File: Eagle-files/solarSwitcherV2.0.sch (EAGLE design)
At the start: 12 parts, among them T1 2N3440

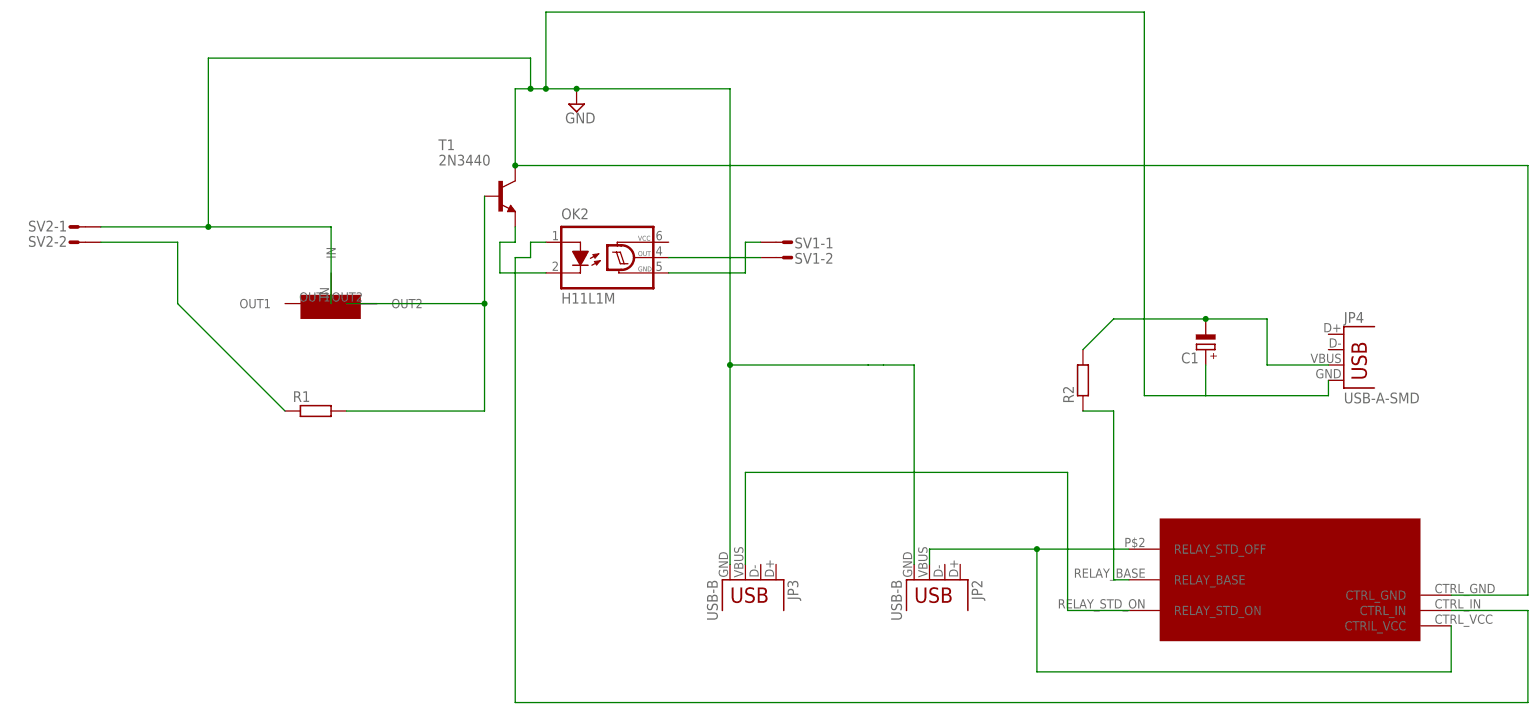
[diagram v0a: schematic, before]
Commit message: Removed relay-board and replaced with seperate relay and diode
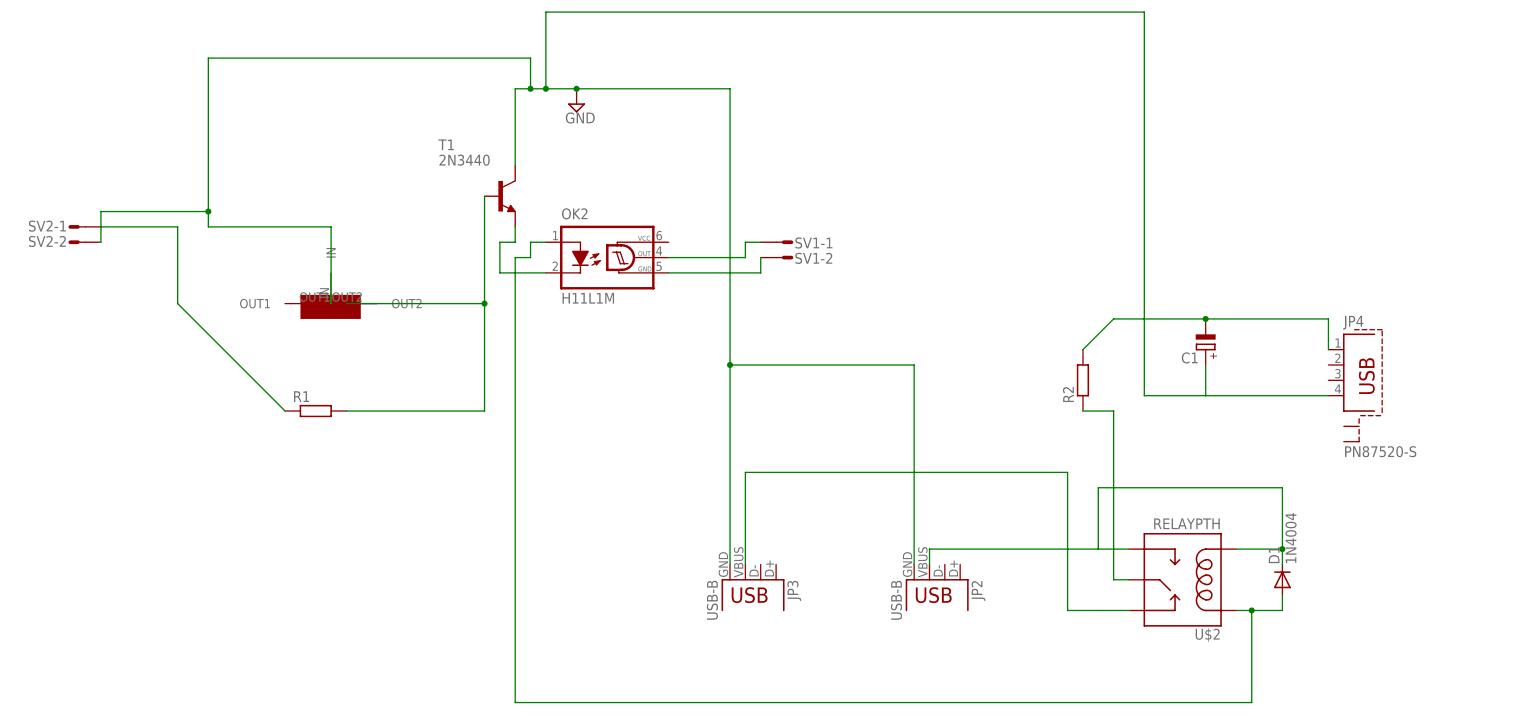
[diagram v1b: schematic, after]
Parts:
- removed U$1: RELAY_BOARD, MBLIB:RELAY_BOARD
- added D1: 1N4004, diode:1N4004
- added U$2: RELAYPTH, SRD-05VDC-SL-C:RELAYPTH
- JP4: value USB-A-SMD -> PN87520-S; device SparkFun-Connectors:USB-A-SMD -> con-berg:PN87520-S
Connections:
- removed net N$9: OK2.OUT, SV1-2.S
- new net N$12: D1.C, JP2.VBUS, U$2.COIL0, U$2.SWOPEN
- net GND: now also SV2-2.S; no longer JP4.GND, SV2-1.S, U$1.CTRL_GND
- net N$10: now also U$2.SWCOMMON; no longer U$1.RELAY_BASE
- net N$2: now also JP4.1; no longer JP4.VBUS
- net N$3: now also D1.A, U$2.COIL1; no longer U$1.CTRL_IN
- net N$4: now also OK2.OUT, SV1-1.S; no longer JP2.VBUS, U$1.CTRIL_VCC, U$1.RELAY_STD_OFF
- net N$5: now also SV2-1.S; no longer SV2-2.S
- net N$6: now also U$2.SWCLOSE; no longer U$1.RELAY_STD_ON
- net N$7: now also SV1-2.S; no longer SV1-1.S

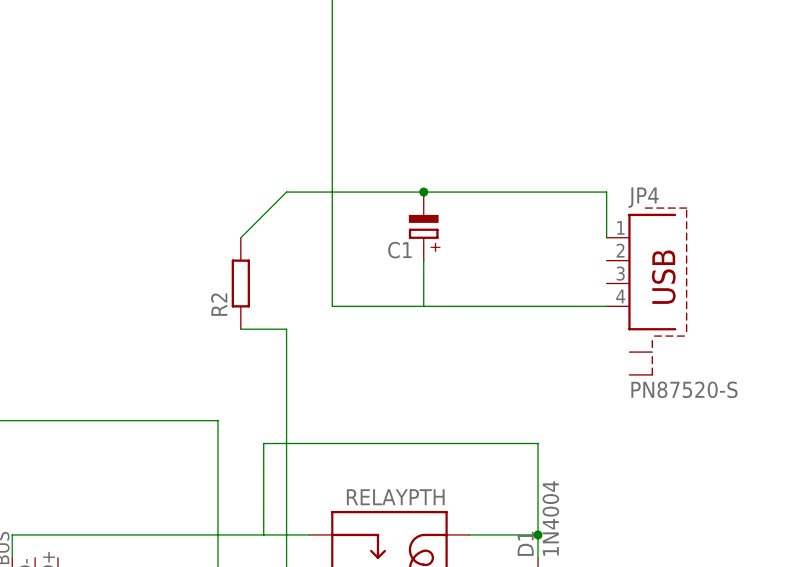
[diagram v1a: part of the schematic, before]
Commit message: Added status leds
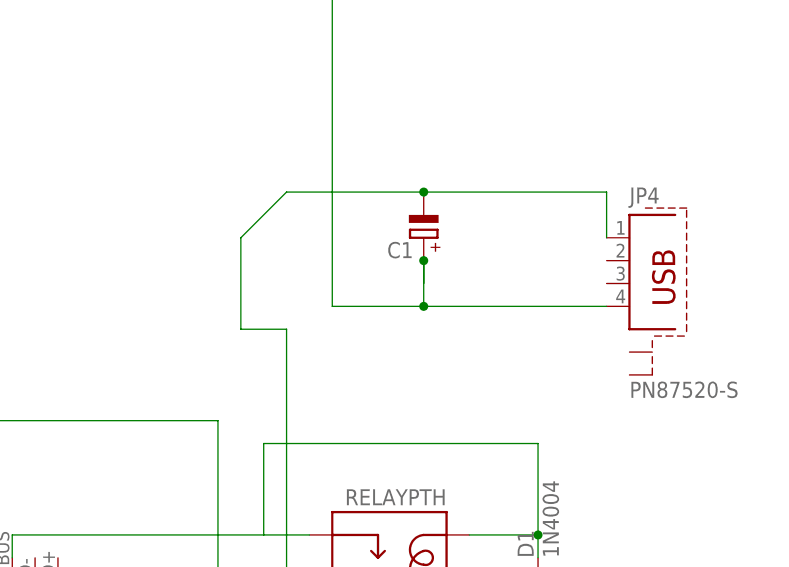
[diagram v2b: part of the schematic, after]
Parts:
- removed R2: (no value), resistor:R-EU_VMTB60
- R1: device resistor:R-EU_VMTB60 -> resistor:R-EU_0207/10
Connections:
- removed net N$10: R2.1, U$2.SWCOMMON
- net GND: now also JP4.4
- net N$2: now also U$2.SWCOMMON; no longer R2.2
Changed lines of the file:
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@@
 <?xml version="1.0" encoding="utf-8"?>
 <!DOCTYPE eagle SYSTEM "eagle.dtd">
-<eagle version="7.3.0">
+<eagle version="7.2.0">
 <drawing>
 <settings>
@@
 <parts>
 <part name="T1" library="transistor" deviceset="2N3440" device=""/>
-<part name="R1" library="resistor" deviceset="R-EU_" device="VMTB60"/>
+<part name="R1" library="resistor" deviceset="R-EU_" device="0207/10"/>
 <part name="SUPPLY3" library="supply2" deviceset="GND" device=""/>
 <part name="JP2" library="SparkFun-Connectors" deviceset="USB" device="PTH" value="USB-B"/>
@@
 <part name="SV2" library="con-amp-mt" deviceset="L02P" device=""/>
 <part name="OK2" library="optocoupler" deviceset="H11L*M" device="" technology="1"/>
-<part name="R2" library="resistor" deviceset="R-EU_" device="VMTB60"/>
 <part name="U$2" library="SRD-05VDC-SL-C" deviceset="RELAY" device="PTH"/>
 <part name="D1" library="diode" deviceset="1N4004" device=""/>
@@
 <instance part="SV2" gate="-2" x="-55.88" y="55.88"/>
 <instance part="OK2" gate="G$1" x="33.02" y="53.34"/>
-<instance part="R2" gate="G$1" x="111.76" y="33.02" rot="R90"/>
 <instance part="U$2" gate="G$1" x="127" y="0" rot="R180"/>
 <instance part="D1" gate="1" x="144.78" y="0" rot="R90"/>
@@
 <junction x="20.32" y="81.28"/>
 <wire x1="121.92" y1="30.48" x2="132.08" y2="30.48" width="0.1524" layer="91"/>
-<wire x1="132.08" y1="30.48" x2="152.4" y2="30.48" width="0.1524" layer="91"/>
-<wire x1="132.08" y1="30.48" x2="132.08" y2="35.56" width="0.1524" layer="91"/>
 <pinref part="C1" gate="G$1" pin="+"/>
 <wire x1="-33.02" y1="86.36" x2="-33.02" y2="60.96" width="0.1524" layer="91"/>
@@
 <wire x1="-50.8" y1="60.96" x2="-50.8" y2="55.88" width="0.1524" layer="91"/>
 <junction x="-33.02" y="60.96"/>
+<wire x1="132.08" y1="30.48" x2="132.08" y2="35.56" width="0.1524" layer="91"/>
+<wire x1="132.08" y1="33.02" x2="132.08" y2="35.56" width="0.1524" layer="91"/>
+<junction x="132.08" y="35.56"/>
+<pinref part="JP4" gate="G$1" pin="4"/>
+<wire x1="152.4" y1="30.48" x2="132.08" y2="30.48" width="0.1524" layer="91"/>
+<junction x="132.08" y="30.48"/>
 </segment>
 </net>
@@
 <junction x="132.08" y="43.18"/>
 <wire x1="116.84" y1="43.18" x2="132.08" y2="43.18" width="0.1524" layer="91"/>
-<pinref part="R2" gate="G$1" pin="2"/>
 <wire x1="111.76" y1="38.1" x2="116.84" y2="43.18" width="0.1524" layer="91"/>
 <pinref part="JP4" gate="G$1" pin="1"/>
 <wire x1="132.08" y1="43.18" x2="152.4" y2="43.18" width="0.1524" layer="91"/>
 <wire x1="152.4" y1="43.18" x2="152.4" y2="38.1" width="0.1524" layer="91"/>
+<wire x1="111.76" y1="27.94" x2="116.84" y2="27.94" width="0.1524" layer="91"/>
+<wire x1="116.84" y1="27.94" x2="116.84" y2="0" width="0.1524" layer="91"/>
+<pinref part="U$2" gate="G$1" pin="SWCOMMON"/>
+<wire x1="119.38" y1="0" x2="116.84" y2="0" width="0.1524" layer="91"/>
+<wire x1="111.76" y1="38.1" x2="111.76" y2="27.94" width="0.1524" layer="91"/>
 </segment>
 </net>
@@
 </segment>
 </net>
-<net name="N$10" class="0">
-<segment>
-<pinref part="R2" gate="G$1" pin="1"/>
-<wire x1="111.76" y1="27.94" x2="116.84" y2="27.94" width="0.1524" layer="91"/>
-<wire x1="116.84" y1="27.94" x2="116.84" y2="0" width="0.1524" layer="91"/>
-<pinref part="U$2" gate="G$1" pin="SWCOMMON"/>
-<wire x1="119.38" y1="0" x2="116.84" y2="0" width="0.1524" layer="91"/>
-</segment>
-</net>

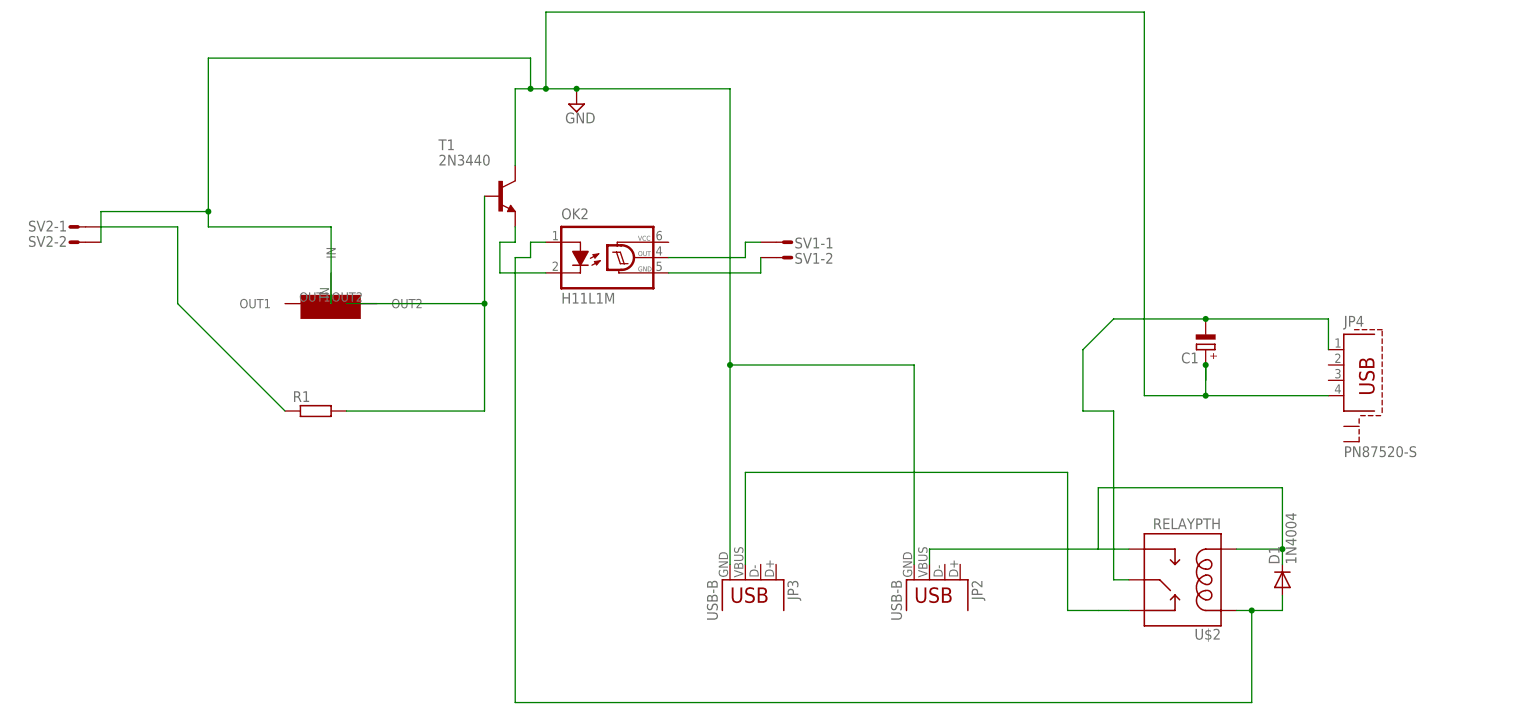
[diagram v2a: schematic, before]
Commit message: Added missing leds
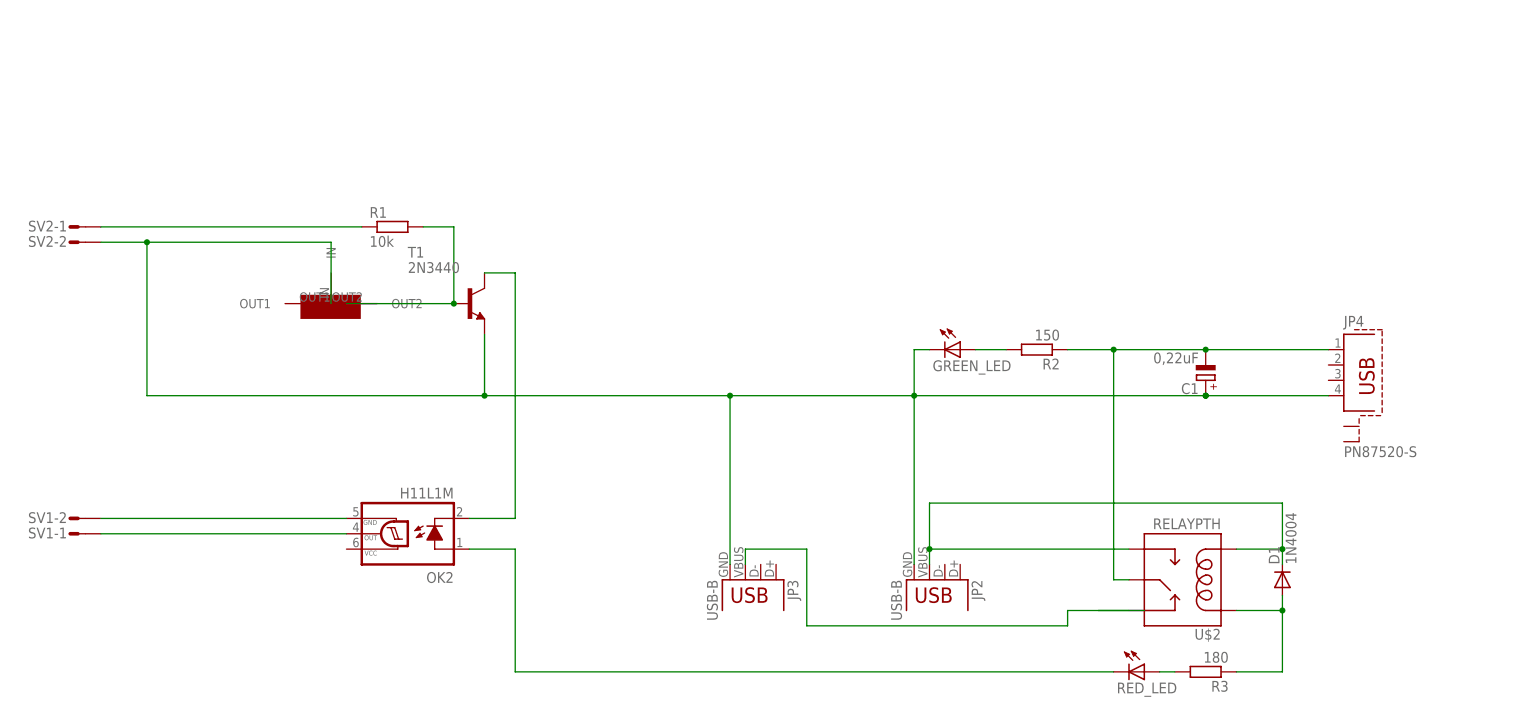
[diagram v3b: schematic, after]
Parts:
- added GREEN_LED, RED_LED: (no value), led:LED5MM
- added R2: 150, resistor:R-EU_0207/10
- added R3: 180, resistor:R-EU_0207/10
- C1: value (none) -> 0,22uF
- R1: value (none) -> 10k
- U$5: value POT_TRIMMER -> 20k
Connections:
- removed net GND: C1.+, JP2.GND, JP3.GND, JP4.4, SV2-2.S, T1.C, U$5.IN
- new net N$10: D1.A, R3.1, U$2.COIL1
- new net N$13: GREEN_LED.A, R2.2
- new net N$14: R3.2, RED_LED.A
- new net N$9: OK2.C, T1.C
- net N$2: now also R2.1
- net N$3: now also RED_LED.C; no longer D1.A, U$2.COIL1
- net N$8: now also C1.+, GREEN_LED.C, JP2.GND, JP3.GND, JP4.4, SV2-2.S, U$5.IN; no longer OK2.C
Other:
- moved on the sheet: C1, OK2, R1, SV1-1, SV1-2, T1
